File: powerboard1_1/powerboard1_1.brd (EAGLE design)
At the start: 149.9 x 86.4 mm, 109 parts, among them Q1 IPP80P03P4L04AKSA1, Q2 2N4401TFR, Q3 2N4401TFR, Q4 2N4401TFR, U1 UWQ-12/20-T48NTB-C, U2 UWE-5/20-Q48NB-C, U3 UWE-3.3/30-Q48NB-C

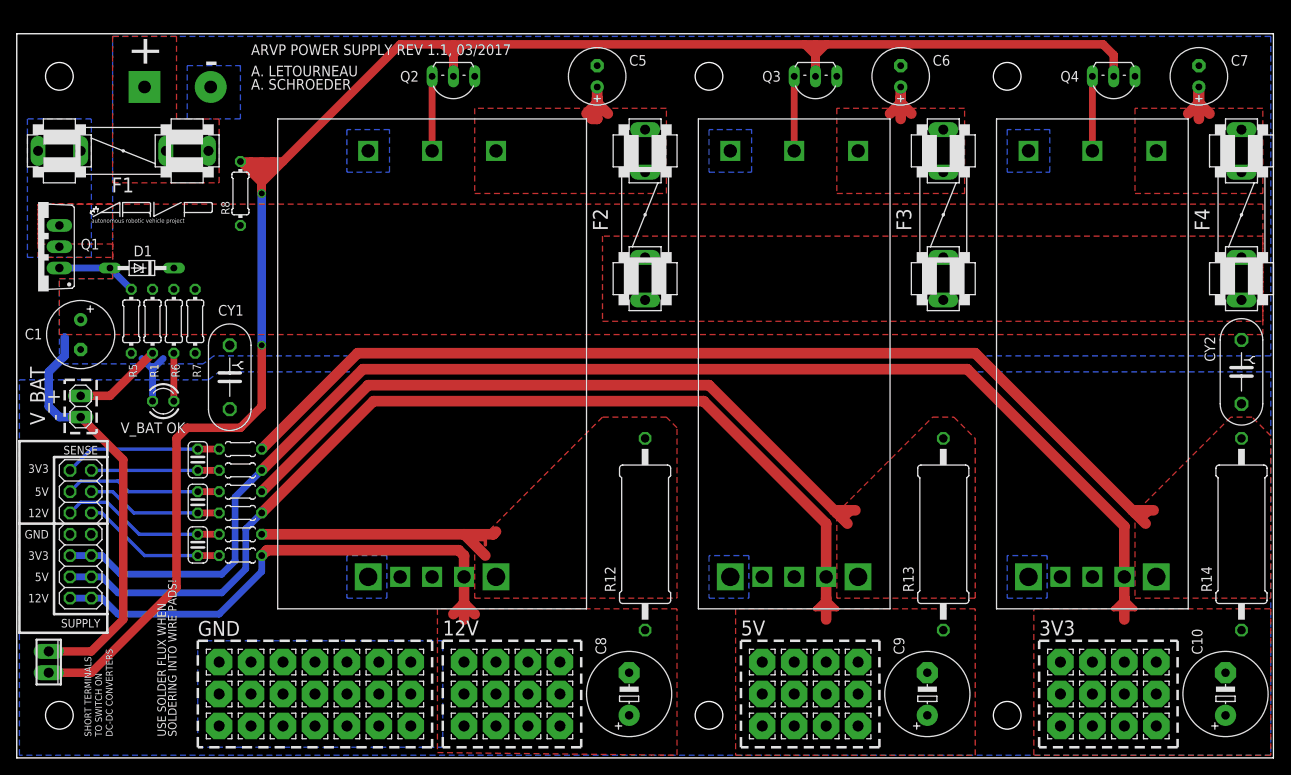
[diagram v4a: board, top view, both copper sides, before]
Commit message: Added low ESR ceramic filtering capacitors; Added open collector style on/off control circuit for each converter; Added more guideline text; Increased clearances beside Q1 to make room for optional heatsink
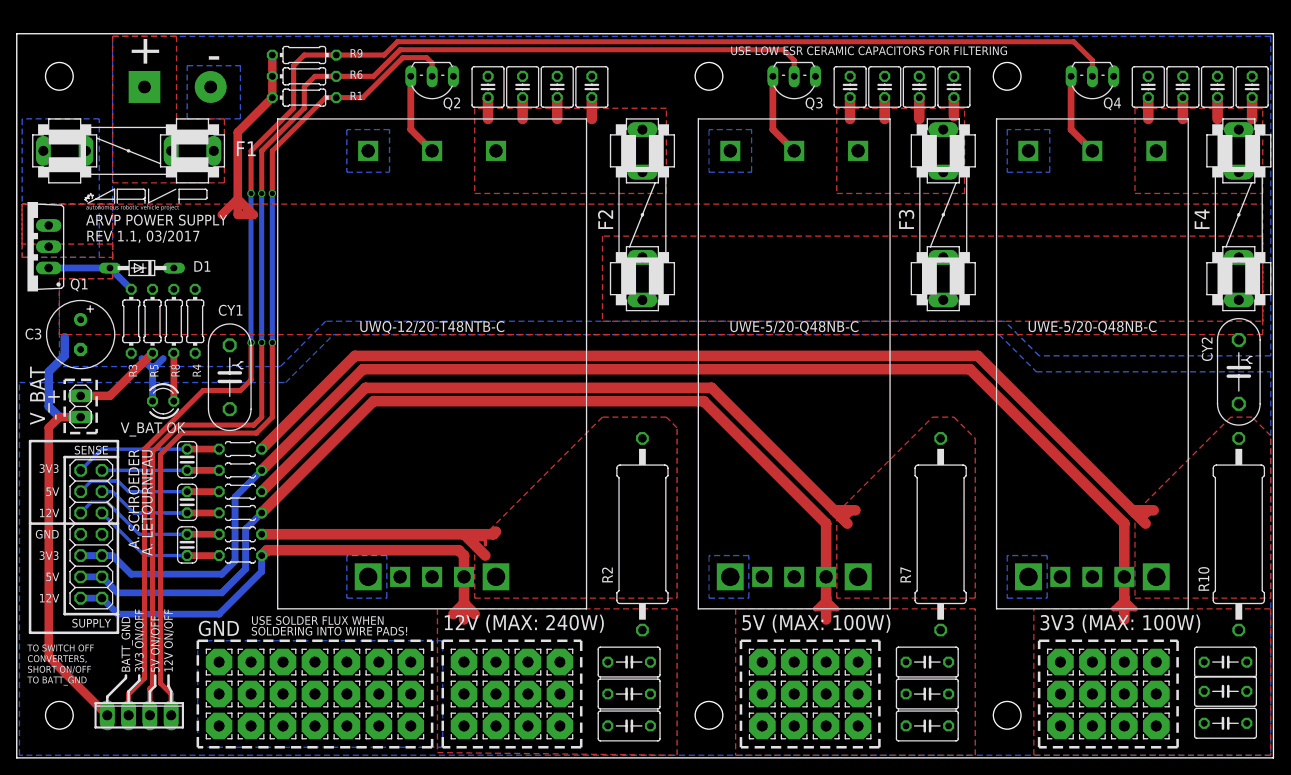
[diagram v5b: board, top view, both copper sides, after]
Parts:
- added C11, C12, C16, C17, C18, C19: (no value), rcl:C025-040X050
- added C13, C14, C15, C20, C21, C22: (no value), rcl:C050-035X075
- added C23, C24, C25: 100n, rcl:C025-024X044
- added R15, R16: 10, rcl:0204/5
- C1: value 100u -> (none); device rcl:E3,5-8 -> rcl:C025-040X050
- C10, C9: device rcl:E5-10,5 -> rcl:C025-040X050
- C2, C4: value 100n -> (none); device rcl:C025-024X044 -> rcl:C025-040X050
- C3: value 100n -> 100u; device rcl:C025-024X044 -> rcl:E3,5-8
- C5: device rcl:E2,5-7 -> rcl:C025-040X050
- C6, C7: device rcl:E2,5-7 -> rcl:C050-035X075
- C8: device rcl:E5-10,5 -> rcl:C050-035X075
- R1: value 4.7k -> 10k
- R10, R2: value 10 -> 0.004; device rcl:0204/5 -> rcl:0617/22
- R12, R13, R14: value 0.004 -> 10; device rcl:0617/22 -> rcl:0204/5
- R3: value 10 -> 2k; device rcl:0204/5 -> resistor:0204/7
- R4: value 10 -> 4.7k; device rcl:0204/5 -> resistor:0204/7
- R5: value 2k -> 4.7k
- R6: value 36k -> 10k
- R7: value 4.7k -> 0.004; device resistor:0204/7 -> rcl:0617/22
- R8: value 4.7k -> 36k
- R9: value 10 -> 10k; device rcl:0204/5 -> resistor:0204/7
- X1: device con-phoenix-254:2POL254 -> con-phoenix-254:4POL254
- moved R14 119.5 mm to (55.9, 22.9), turned to 0 degrees
- moved R10 119.2 mm to (174.9, 17.8), turned to 270 degrees
- moved PAD19 108.2 mm to (161.3, -5.08)
- moved PAD9 100.4 mm to (161.3, 2.54)
- moved C7 100.2 mm to (102.2, -1.27), turned to 0 degrees
- moved PAD4 96.5 mm to (165.1, 2.54)
- moved PAD14 92.7 mm to (165.1, -5.08)
- moved R7 92.5 mm to (139.4, 17.8)
- moved PAD46 89.0 mm to (76.2, -1.27)
- moved PAD50 89.0 mm to (68.6, -1.27)
- moved R13 83.9 mm to (55.9, 20.3), turned to 180 degrees
- moved PAD51 81.4 mm to (72.4, -1.27)
- moved C10 81.1 mm to (136.8, 71.1)
- moved PAD55 78.7 mm to (82.5, -1.27)
- moved C6 77.0 mm to (102.2, 2.54), turned to 0 degrees
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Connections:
- removed net N$13: C7.+, F4.2A, F4.2B, U3.+VIN
- removed net N$9: C6.+, F3.2A, F3.2B, U2.+VIN
- removed net ON/OFF: Q2.B, Q3.B, Q4.B, R8.2, X1.2
- new net N$12: C16.1, C17.1, C18.1, C19.1, F4.2A, F4.2B, U3.+VIN
- new net N$7: C10.1, C11.1, C12.1, C9.1, F3.2A, F3.2B, U2.+VIN
- new net ON/OFF_1: Q2.B, R1.2, X1.4
- new net ON/OFF_2: Q3.B, R6.2, X1.3
- new net ON/OFF_3: Q4.B, R9.2, X1.2
- net 12V+SENSE: now also R12.2, R2.1; no longer R12.1, R9.2
- net 12V-SENSE: now also C6.1, C7.1, C8.1, PAD12.1, PAD17.1, PAD2.1, PAD37.1, PAD42.1, PAD47.1, PAD52.1, PAD55.1, PAD7.1, R11.1, R2.2; no longer C8.+, PAD23.1, PAD24.1, PAD25.1, PAD26.1, PAD28.1, PAD29.1, PAD30.1, PAD31.1, PAD33.1, R12.2, R2.1
- net 3V3+SENSE: now also R10.1, R16.2; no longer R11.2, R14.1
- net 3V3-SENSE: now also C20.1, C21.1, C22.1, PAD14.1, PAD19.1, PAD24.1, PAD29.1, PAD34.1, PAD39.1, PAD4.1, PAD44.1, PAD9.1, R10.2, R15.1; no longer C10.+, PAD46.1, PAD47.1, PAD48.1, PAD50.1, PAD51.1, PAD52.1, PAD53.1, PAD55.1, PAD56.1, R14.2, R4.1
- net 5V+SENSE: now also R14.2, R7.1; no longer R10.2, R13.1
- net 5V-SENSE: now also C13.1, C14.1, C15.1, PAD13.1, PAD18.1, PAD23.1, PAD28.1, PAD3.1, PAD33.1, PAD48.1, PAD53.1, PAD56.1, PAD8.1, R13.1, R7.2; no longer C9.+, PAD34.1, PAD35.1, PAD36.1, PAD37.1, PAD39.1, PAD40.1, PAD41.1, PAD42.1, PAD44.1, PAD45.1, R13.2, R3.1
- net GND: now also C13.2, C14.2, C15.2, C20.2, C21.2, C22.2, C6.2, C7.2, C8.2, PAD25.1, PAD26.1, PAD30.1, PAD31.1, PAD35.1, PAD36.1, PAD40.1, PAD41.1, PAD45.1, PAD46.1, PAD50.1, PAD51.1; no longer C10.-, C8.-, C9.-, PAD12.1, PAD13.1, PAD14.1, PAD17.1, PAD18.1, PAD19.1, PAD2.1, PAD3.1, PAD4.1, PAD7.1, PAD8.1, PAD9.1
- net J3: now also C25.1, R11.2; no longer C4.1, R2.2
- net J4: now also C25.2, R12.1; no longer C4.2, R9.1
- net J5: now also C24.1, R13.2; no longer C3.1, R3.2
- net J6: now also C24.2, R14.1; no longer C3.2, R10.1
- net J7: now also C23.1, R15.2; no longer C2.1, R4.2
- net J8: now also C23.2, R16.1; no longer C2.2, R11.1
- net N$1: now also R8.1; no longer R6.1
- net N$2: now also R5.2; no longer R1.2
- net N$4: now also R3.1; no longer R5.1
- net N$5: now also C1.1, C2.1, C4.1, C5.1; no longer C5.+
- net V+: now also C3.+, R4.1, R5.1, R6.1, R8.2, R9.1; no longer C1.+, R6.2, R7.1, R8.1
- net V-: now also C1.2, C10.2, C11.2, C12.2, C16.2, C17.2, C18.2, C19.2, C2.2, C3.-, C4.2, C5.2, C9.2, R3.2, R4.2; no longer C1.-, C5.-, C6.-, C7.-, R5.2, R7.2
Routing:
- net ON/OFF: track 225.6 -> 0.00 mm, vias 2 -> 0
- net ON/OFF_3: track 0.00 -> 187.5 mm, vias 0 -> 2
- net ON/OFF_2: track 0.00 -> 150.5 mm, vias 0 -> 2
- net ON/OFF_1: track 0.00 -> 104.1 mm, vias 0 -> 2
- net V+: track 0.00 -> 28.1 mm
- net N$12: track 0.00 -> 10.2 mm
- net N$7: track 0.00 -> 9.84 mm
- net N$13: track 9.31 -> 0.00 mm
- net N$9: track 7.40 -> 0.00 mm
- net V-: track 57.8 -> 62.6 mm
- net N$4: track 9.62 -> 10.9 mm
- net J8: track 18.8 -> 17.6 mm
- net J7: track 15.2 -> 14.0 mm
- net J6: track 18.8 -> 17.6 mm
- net J5: track 16.3 -> 15.0 mm
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- added copper zone on layer 1, net N$12
- added copper zone on layer 1, net N$7
- removed copper zone on layer 1, net N$13
- removed copper zone on layer 1, net N$9
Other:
- board text added: "12V (MAX: 240W)"
- board text added: "12V ON/OFF"
- board text added: "3V3 (MAX: 100W)"
- board text added: "3V3 ON/OFF"
- board text added: "5V (MAX: 100W)"
- board text added: "5V ON/OFF"
- board text added: "ARVP POWER SUPPLY"
- board text added: "BATT_GND"
- board text added: "CONVERTERS,"
- board text added: "REV 1.1, 03/2017"
- board text added: "SHORT ON/OFF"
- board text added: "TO BATT_GND"
- board text added: "TO SWITCH OFF"
- board text added: "USE LOW ESR CERAMIC CAPACITORS FOR FILTERING"
- board text added: "UWE-5/20-Q48NB-C"
- board text added: "UWQ-12/20-T48NTB-C"
- board text removed: "ARVP POWER SUPPLY REV 1.1, 03/2017"
- board text removed: "DC-DC CONVERTERS"
- board text removed: "SHORT TERMINALS"
- board text removed: "TO SWITCH ON"

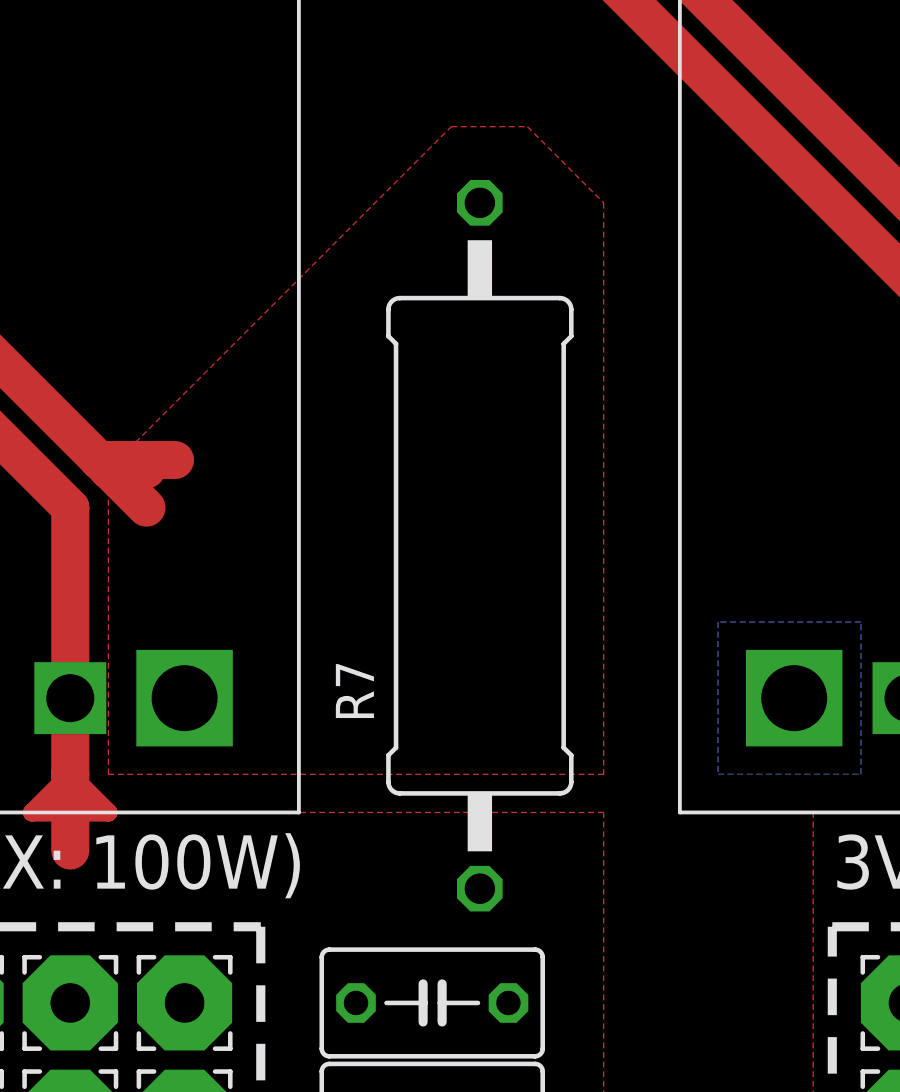
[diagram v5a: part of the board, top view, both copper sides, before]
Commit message: Adjusted position of R7
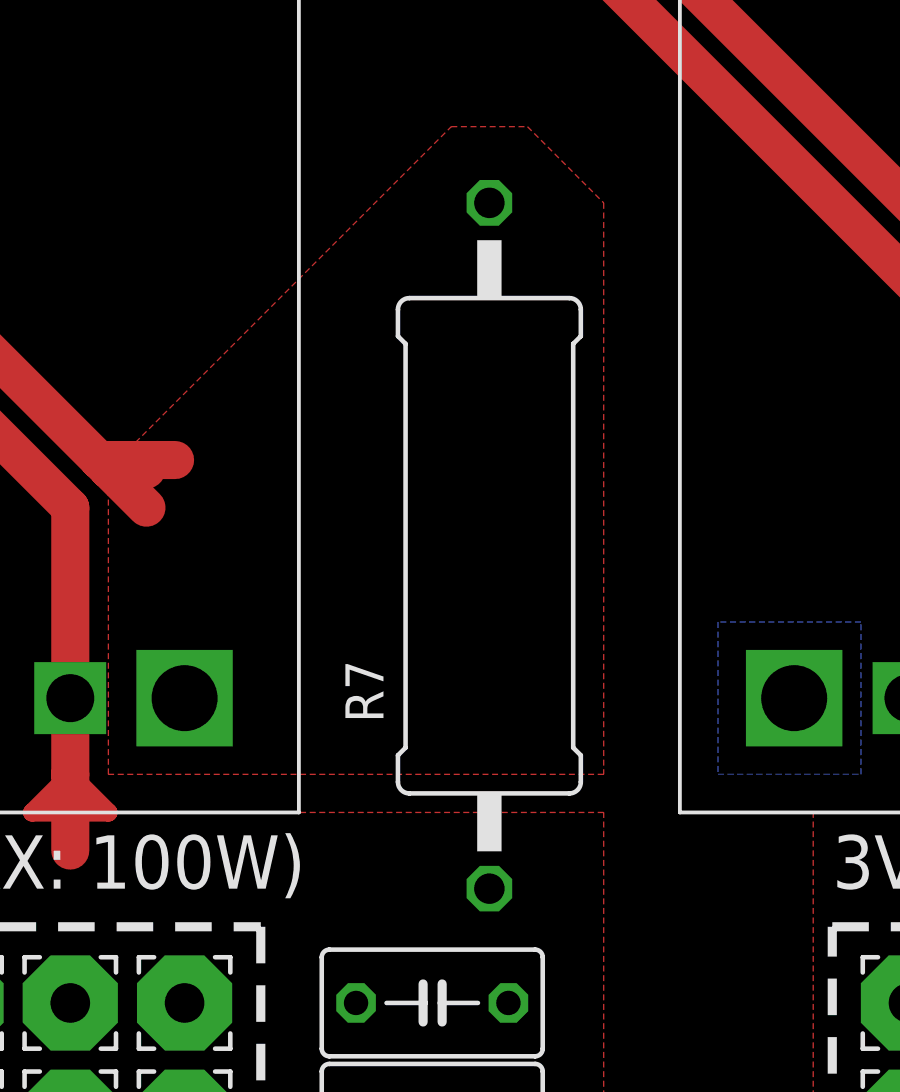
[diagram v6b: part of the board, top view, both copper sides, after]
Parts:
- moved R7 0.32 mm to (139.7, 17.8)
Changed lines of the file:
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@@
 <attribute name="VALUE" x="103.2383" y="24.257" size="1.27" layer="27" ratio="10" rot="R270"/>
 </element>
-<element name="R7" library="rcl" package="0617/22" value="0.004" x="139.3825" y="17.78" smashed="yes" rot="R270">
-<attribute name="NAME" x="134.5819" y="13.97" size="1.27" layer="25" ratio="10" rot="R270"/>
-<attribute name="VALUE" x="138.7983" y="24.257" size="1.27" layer="27" ratio="10" rot="R270"/>
+<element name="R7" library="rcl" package="0617/22" value="0.004" x="139.7" y="17.78" smashed="yes" rot="R270">
+<attribute name="NAME" x="134.8994" y="13.97" size="1.27" layer="25" ratio="10" rot="R270"/>
+<attribute name="VALUE" x="139.1158" y="24.257" size="1.27" layer="27" ratio="10" rot="R270"/>
 </element>
 <element name="R10" library="rcl" package="0617/22" value="0.004" x="174.9425" y="17.78" smashed="yes" rot="R270">
